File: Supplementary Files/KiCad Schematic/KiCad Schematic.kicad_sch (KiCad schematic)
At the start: 8 parts, among them U1 ESP32-S3-WROOM-1

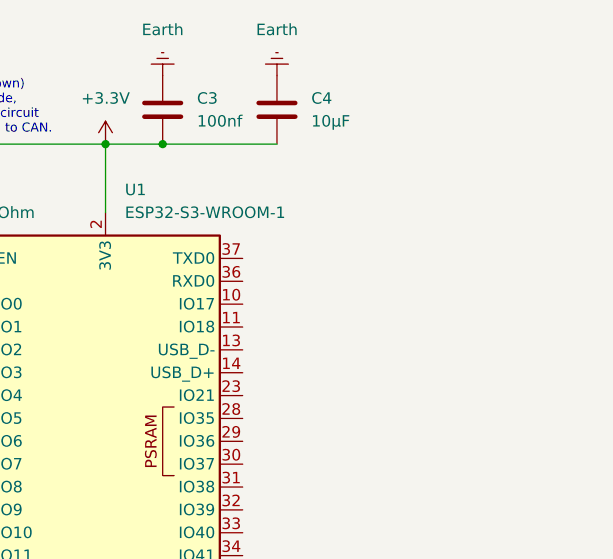
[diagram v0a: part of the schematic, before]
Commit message: KiCad added connections to J17 expansion module.
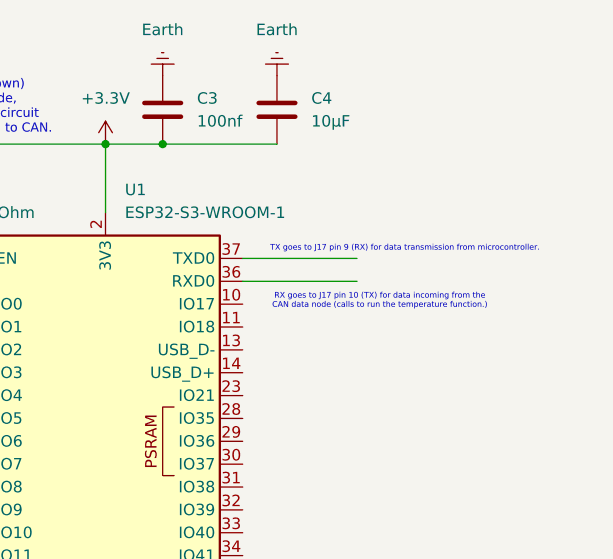
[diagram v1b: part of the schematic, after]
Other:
- note added: "RX goes to J17 pin 10 (TX) for data incoming from the CAN data node (calls to run the temperature function.)"
- note added: "TX goes to J17 pin 9 (RX) for data transmission from microcontroller."
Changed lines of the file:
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@@
+		)
+	)
+	(text "TX goes to J17 pin 9 (RX) for data transmission from microcontroller."
+		(exclude_from_sim no)
+		(at 147.574 39.624 0)
+		(effects
+			(font
+				(size 0.635 0.635)
+			)
 		)
 	)
@@
 			(font
 				(size 1.016 1.016)
+			)
+		)
+	)
+	(text "RX goes to J17 pin 10 (TX) for data incoming from the\nCAN data node (calls to run the temperature function.)"
+		(exclude_from_sim no)
+		(at 144.78 45.466 0)
+		(effects
+			(font
+				(size 0.635 0.635)
 			)
 		)
@@
 		)
 	)
+	(wire
+		(pts
+			(xy 129.54 40.64) (xy 142.24 40.64)
+		)
+		(stroke
+			(width 0)
+			(type default)
+		)
+	)
 	(polyline
 		(pts
@@
 		)
 		(stroke
+			(width 0)
+			(type default)
+		)
+	)
+	(wire
+		(pts
+			(xy 129.54 43.18) (xy 142.24 43.18)
+		)
+		(stroke
